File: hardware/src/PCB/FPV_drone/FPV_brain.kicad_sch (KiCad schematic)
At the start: 33 parts, among them IC2 STM32H743VIT6, IC3 USBLC6-2SC6, J1 TYPE-C-31-M-12, J3 Flash-pads, Y1 ABM3B-8.000MHZ-10-D1G-T

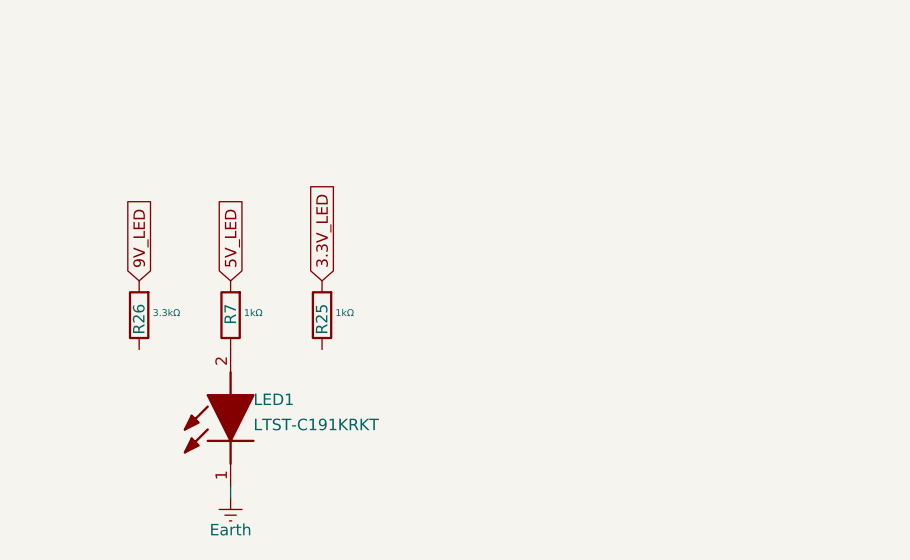
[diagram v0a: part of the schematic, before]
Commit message: added some leds
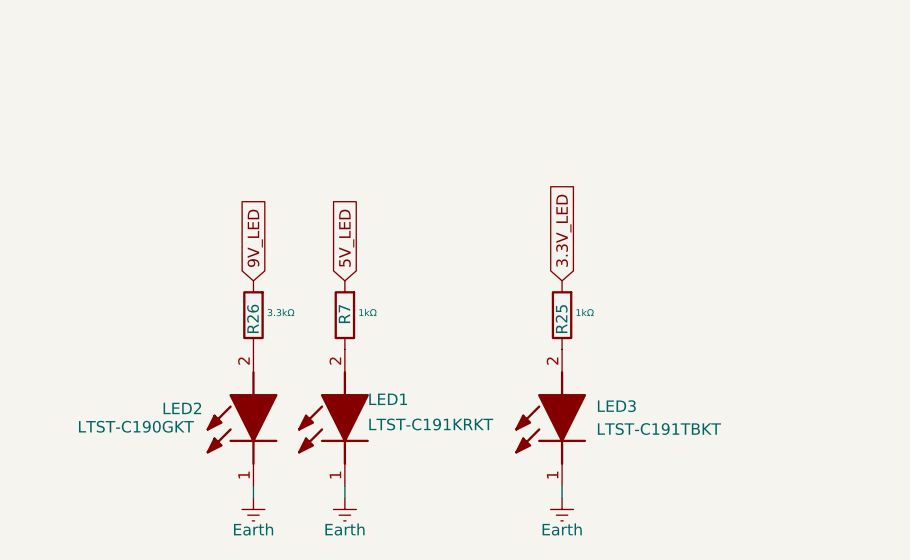
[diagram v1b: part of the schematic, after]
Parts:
- added LED2: LTST-C190GKT, LEDC1608X90N, symbol lib:LTST-C190GKT
- added LED3: LTST-C191TBKT, LEDC1608X65N, symbol lib:LTST-C191TBKT
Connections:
- net Earth: now also LED2.1 (K), LED3.1 (K)
- net at R26.1: now also LED2.2 (A)
- net at R25.1: now also LED3.2 (A)
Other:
- moved on the sheet: LED1, R25, R26, R7

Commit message: Update: schem drone
power functions almost finish... i wish
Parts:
- removed IC3: USBLC6-2SC6, SOT95P280X145-6N, symbol lib:USBLC6-2SC6
- removed J1: TYPE-C-31-M-12, TYPE-C-31-M-12:HRO_TYPE-C-31-M-12, symbol lib:TYPE-C-31-M-12
- removed J3: Flash-pads, symbol Connector_Generic:Conn_01x05
- removed R1, R2: 5.1kΩ, symbol Device:R
- added H1, H2, H3, H4: MountingHole_Pad, symbol Mechanical:MountingHole_Pad
- added TP1, TP2, TP3, TP4, TP5: TestPoint, symbol Connector:TestPoint
- C1, C2: value 15pF -> 12pF
- FB1: value BLM18BD421SZ1D (inductance) -> 220Ω @ 100MHz
- R12, R17: value 100Ω -> 10kΩ
- R25: value 1kΩ -> 680Ω
- R26: value 3.3kΩ -> 4.7kΩ
- R7: value 1kΩ -> 2.2kΩ
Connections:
- net 3.3V_LED is gone; now on net MCU_LED: R25.2
- net +3.3V: now also IC2.6 (VBAT), TP4.1
- net Earth: now also H1.1, H2.1, H3.1, H4.1, TP5.1
- net NRST: now also TP3.1
- net SWCLK: now also TP2.1
- net SWDIO: now also TP1.1
- net MCU_LED: now reaches IC2.34 (PB0)
- net 5V_LED renamed +5V
- net 9V_LED renamed +9V
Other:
- moved on the sheet: C1, C10, C11, C2, C22, C23, C24, C3, C4, C5, C6, C7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

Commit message: Update: schem almost finish
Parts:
- removed C22, C23, C24: 100nF, Capacitor_THT:C_Disc_D3.0mm_W2.0mm_P2.50mm, symbol PCM_SL_Devices:Capacitor_NP
- removed FB1: 220Ω @ 100MHz, BLM18SP221SN1B, symbol lib:BLM18BD421SZ1D
- removed R12, R17, R8: 10kΩ, symbol Device:R
- added C54: 100nF, Capacitor_THT:C_Disc_D3.0mm_W2.0mm_P2.50mm, symbol PCM_SL_Devices:Capacitor_NP
- added FB1: 220Ω @ 100MHz, BLM18SP221SN1B, symbol Device:L
- added J10, J7, J8, J9: JST_1mm_3, PCM_SparkFun-Connector:JST_1x03_P1.0mm_Horizontal_SMD, symbol PCM_SparkFun-Connector:Conn_01x03_JST_P1.0mm_Horizontal_SMD
- added J2: Conn_01x08, PCM_SparkFun-Connector:JST_1x08_P1.0mm_Horizontal_SMD, symbol PCM_SparkFun-Connector:Conn_01x08_JST_P1.0mm_Horizontal_SMD
- added J4: JST_1mm_4, PCM_SparkFun-Connector:JST_1x04_P1.0mm_Horizontal_SMD, symbol PCM_SparkFun-Connector:Conn_01x04_JST_P1.0mm_Horizontal_SMD
- added NT2: NetTie_4_Cross, symbol Device:NetTie_4_Cross
- added R40: 47Ω, symbol Device:R
- added R41: 10kΩ, symbol Device:R
- R25: value 680Ω -> 220Ω
- R26: value 4.7kΩ -> 1.1kΩ
- R7: value 2.2kΩ -> 620Ω
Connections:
- net +3.3V: now also FB1.1, R41.1
- net +5V: now also J4.3
- net Earth: now also C54.2, J2.1, J4.4, NT2.3; no longer IC2.19 (VSSA)
- net IBAT: now also IC2.25 (PA3)
- net ISC_IN: now also C1.2, Y1.1 (XTAL_1); no longer C2.1, Y1.3 (XTAL_2)
- net ISC_OUT: now also C2.1, Y1.3 (XTAL_2); no longer C1.2, Y1.1 (XTAL_1)
- net VBAT: now also IC2.24 (PA2)
- net at LED3.2 (A): now also R26.1; no longer R25.1
- net at LED2.2 (A): now also R25.1; no longer R26.1
- net CURR: now reaches IC2.15 (PC0)
- net CURR: now also J2.8
- net VDDA: now reaches IC2.21 (VDDA)
- net VDDA: now also FB1.2, R40.1; no longer IC2.20 (VREF+)
- net IMU1_CS: now reaches IC2.28 (PA4)
- net IMU1_SCLK: now reaches IC2.29 (PA5)
- net IMU1_SDO: now reaches IC2.30 (PA6)
- net IMU1_SDIO: now reaches IC2.31 (PA7)
- net IMU1_INT: now reaches IC2.32 (PC4)
- net IMU2_CS: now reaches IC2.35 (PB1)
- net IMU2_INT: now reaches IC2.36 (PB2)
- net IMU2_SCLK: now reaches IC2.42 (PE12)
- net IMU2_SDO: now reaches IC2.43 (PE13)
- net IMU2_SDIO: now reaches IC2.44 (PE14)
- net SCL: now reaches IC2.46 (PB10)
- net SDA: now reaches IC2.47 (PB11)
- net OSD_CS: now reaches IC2.51 (PB12)
- net OSD_SCK: now reaches IC2.52 (PB13)
- net OSD_MISO: now reaches IC2.53 (PB14)
- net OSD_MOSI: now reaches IC2.54 (PB15)
- net DJI_TX: now reaches IC2.55 (PD8)
- net DJI_RX: now reaches IC2.56 (PD9)
- net MOTOR_1: now reaches IC2.59 (PD12)
- net MOTOR_1: now also J2.3
- net MOTOR_2: now reaches IC2.60 (PD13)
- net MOTOR_2: now also J2.4
- net MOTOR_3: now reaches IC2.61 (PD14)
- net MOTOR_3: now also J2.5
- net MOTOR_4: now reaches IC2.62 (PD15)
- net MOTOR_4: now also J2.6
- net flash_CS: now reaches IC2.77 (PA15)
- net flash_CLK: now reaches IC2.78 (PC10)
- net flash_MISO: now reaches IC2.79 (PC11)
- net flash_MOSI: now reaches IC2.80 (PC12)
- net RADIO_RX: now reaches IC2.81 (PD0)
- net RADIO_RX: now also J4.2
- net RADIO_TX: now reaches IC2.82 (PD1)
- net RADIO_TX: now also J4.1
- net DJI_SBUS: now reaches IC2.87 (PD6)
- net TELE: now reaches IC2.93 (PB7)
- net TELE: now also J2.7
- net NRST renamed B_NRST
- net B_NRST: now also C54.1, R41.2
- new net BATT+: J2.2
- new net GNDA: IC2.19 (VSSA), NT2.2
- new net GNDD: NT2.4
- new net GNDPWR: NT2.1
- new net VREF: IC2.20 (VREF+), R40.2
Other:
- note added: "Advanced VDDA filtering"
- note added: "Blue - 9V Red - 5V Green - MCU (3.3V)"
- note added: "CL_reel = (C1*C2)/(C1+C2) + C_stray = (12*12)/(12+12) + ~3pF = 6 + 3 = 9-10 pF"
- note added: "Connectors"
- note added: "Crystal 0scillator - 8MHz +/-10ppm 200Ω 10pF"
- note added: "Info LEDS"
- note added: "Microcontroller - STM32H743VIT6"
- note added: "Mounting Holes"
- note added: "NRST button logic"
- moved on the sheet: C1, C10, C11, C2, C3, C4, C5, C6, C7, C8, C9, H1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

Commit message: Update: bit changes
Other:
- moved on the sheet: NT2
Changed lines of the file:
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@@
 	(wire
 		(pts
-			(xy 104.14 146.05) (xy 105.41 146.05)
+			(xy 77.47 143.51) (xy 78.74 143.51)
 		)
 		(stroke
@@
 	(wire
 		(pts
-			(xy 107.95 142.24) (xy 107.95 143.51)
+			(xy 81.28 139.7) (xy 81.28 140.97)
 		)
 		(stroke
@@
 	(wire
 		(pts
-			(xy 110.49 146.05) (xy 111.76 146.05)
+			(xy 83.82 143.51) (xy 85.09 143.51)
 		)
 		(stroke
@@
 	(wire
 		(pts
-			(xy 107.95 148.59) (xy 107.95 149.86)
+			(xy 81.28 146.05) (xy 81.28 147.32)
 		)
 		(stroke
@@
 	(symbol
 		(lib_id "power:Earth")
-		(at 107.95 142.24 180)
+		(at 81.28 139.7 180)
 		(unit 1)
 		(body_style 1)
@@
 		(dnp no)
 		(property "Reference" "#PWR0114"
-			(at 107.95 135.89 0)
+			(at 81.28 133.35 0)
 			(hide yes)
 			(show_name no)
@@
 		)
 		(property "Value" "Earth"
-			(at 107.95 138.684 0)
+			(at 81.28 136.144 0)
 			(show_name no)
 			(do_not_autoplace no)
@@
 		)
 		(property "Footprint" ""
-			(at 107.95 142.24 0)
+			(at 81.28 139.7 0)
 			(hide yes)
 			(show_name no)
@@
 		)
 		(property "Datasheet" ""
-			(at 107.95 142.24 0)
+			(at 81.28 139.7 0)
 			(hide yes)
 			(show_name no)
@@
 		)
 		(property "Description" "Power symbol creates a global label with name \"Earth\""
-			(at 107.95 142.24 0)
+			(at 81.28 139.7 0)
 			(hide yes)
 			(show_name no)
@@
 	(symbol
 		(lib_id "Device:NetTie_4_Cross")
-		(at 107.95 146.05 0)
+		(at 81.28 143.51 0)
 		(unit 1)
 		(body_style 1)
@@
 		(dnp no)
 		(property "Reference" "NT2"
-			(at 103.124 150.114 0)
+			(at 76.454 147.574 0)
 			(show_name no)
 			(do_not_autoplace no)
@@
 		)
 		(property "Value" "NetTie_4_Cross"
-			(at 118.11 143.6368 0)
+			(at 91.44 141.0968 0)
 			(hide yes)
 			(show_name no)
@@
 		)
 		(property "Footprint" ""
-			(at 107.95 146.05 0)
+			(at 81.28 143.51 0)
 			(hide yes)
 			(show_name no)
@@
 		)
 		(property "Datasheet" ""
-			(at 107.95 146.05 0)
+			(at 81.28 143.51 0)
 			(hide yes)
 			(show_name no)
@@
 		)
 		(property "Description" "Net tie, 4 pins, cross"
-			(at 107.95 146.05 0)
+			(at 81.28 143.51 0)
 			(hide yes)
 			(show_name no)
@@
 	(symbol
 		(lib_id "power:GNDD")
-		(at 107.95 149.86 0)
+		(at 81.28 147.32 0)
 		(unit 1)
 		(body_style 1)
@@
 		(dnp no)
 		(property "Reference" "#PWR0117"
-			(at 107.95 156.21 0)
+			(at 81.28 153.67 0)
 			(hide yes)
 			(show_name no)
@@
 		)
 		(property "Value" "GNDD"
-			(at 107.95 153.162 0)
+			(at 81.28 150.622 0)
 			(show_name no)
 			(do_not_autoplace no)
@@
 		)
 		(property "Footprint" ""
-			(at 107.95 149.86 0)
+			(at 81.28 147.32 0)
 			(hide yes)
 			(show_name no)
@@
 		)
 		(property "Datasheet" ""
-			(at 107.95 149.86 0)
+			(at 81.28 147.32 0)
 			(hide yes)
 			(show_name no)
@@
 		)
 		(property "Description" "Power symbol creates a global label with name \"GNDD\" , digital ground"
-			(at 107.95 149.86 0)
+			(at 81.28 147.32 0)
 			(hide yes)
 			(show_name no)
@@
 	(symbol
 		(lib_id "power:GNDPWR")
-		(at 104.14 146.05 270)
+		(at 77.47 143.51 270)
 		(unit 1)
 		(body_style 1)
@@
 		(dnp no)
 		(property "Reference" "#PWR0118"
-			(at 99.06 146.05 0)
+			(at 72.39 143.51 0)
 			(hide yes)
 			(show_name no)
@@
 		)
 		(property "Value" "GNDPWR"
-			(at 98.298 145.796 90)
+			(at 71.628 143.256 90)
 			(show_name no)
 			(do_not_autoplace no)
@@
 		)
 		(property "Footprint" ""
-			(at 102.87 146.05 0)
+			(at 76.2 143.51 0)
 			(hide yes)
 			(show_name no)
@@
 		)
 		(property "Datasheet" ""
-			(at 102.87 146.05 0)
+			(at 76.2 143.51 0)
 			(hide yes)
 			(show_name no)
@@
 		)
 		(property "Description" "Power symbol creates a global label with name \"GNDPWR\" , global ground"
-			(at 104.14 146.05 0)
+			(at 77.47 143.51 0)
 			(hide yes)
 			(show_name no)
@@
 	(symbol
 		(lib_id "power:GNDA")
-		(at 111.76 146.05 90)
+		(at 85.09 143.51 90)
 		(unit 1)
 		(body_style 1)
@@
 		(dnp no)
 		(property "Reference" "#PWR0119"
-			(at 118.11 146.05 0)
+			(at 91.44 143.51 0)
 			(hide yes)
 			(show_name no)
@@
 		)
 		(property "Value" "GNDA"
-			(at 116.586 146.05 90)
+			(at 89.916 143.51 90)
 			(show_name no)
 			(do_not_autoplace no)
@@
 		)
 		(property "Footprint" ""
-			(at 111.76 146.05 0)
+			(at 85.09 143.51 0)
 			(hide yes)
 			(show_name no)
@@
 		)
 		(property "Datasheet" ""
-			(at 111.76 146.05 0)
+			(at 85.09 143.51 0)
 			(hide yes)
 			(show_name no)
@@
 		)
 		(property "Description" "Power symbol creates a global label with name \"GNDA\" , analog ground"
-			(at 111.76 146.05 0)
+			(at 85.09 143.51 0)
 			(hide yes)
 			(show_name no)

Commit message: update: schem finished
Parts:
- removed C11: 1uF, Capacitor_THT:C_Disc_D3.0mm_W2.0mm_P2.50mm, symbol PCM_SL_Devices:Capacitor_NP
- removed FB1: 220Ω @ 100MHz, BLM18SP221SN1B, symbol Device:L
- removed IC2: STM32H743VIT6, QFP50P1600X1600X160-100N, symbol lib:STM32H743VIT6
- removed R9: 10kΩ, symbol Device:R
- added C14: 2.2uF, Capacitor_THT:C_Disc_D3.0mm_W2.0mm_P2.50mm, symbol PCM_SL_Devices:Capacitor_NP
- added L3: STM32H743VIH6, LIB:BGA100C80P10X10_800X800X110, symbol lib:STM32H743VIH6
- C10: value 100nF -> 1uF
- C5: value 2.2uF -> 4.7uF
- H1, H2, H3, H4: footprint (none) -> MountingHole:MountingHole_3.2mm_M3_ISO7380_Pad_TopBottom
- LED1: footprint LEDC1608X55N -> LIB:LEDC1608X55N
- LED2: footprint LEDC1608X90N -> LIB:LEDC1608X90N
- LED3: footprint LEDC1608X65N -> LIB:LEDC1608X65N
- NT2: footprint (none) -> NetTie:NetTie-4_SMD_Pad0.5mm
- R40: value 47Ω -> 10kΩ
- S2: footprint EVQ-P7A01P:SW_EVQ-P7A01P -> LIB:SW_EVQ-P7A01P
- TP1, TP2, TP3, TP4, TP5: footprint (none) -> TestPoint:TestPoint_Pad_D1.0mm
- Y1: footprint ABM3B -> LIB:ABM3B
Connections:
- net VDDA is gone; now on net Earth: R40.1
- net VREF is gone; now on net STM_BOOT0: R40.2
- net +3.3V: now also C10.1, C4.1, C5.1, C8.1, C9.1, L3.B2 (VBAT), L3.D2 (VDD_1), L3.F4 (VDDLDO), L3.F5 (VDD_2), L3.F6 (VDD33USB), L3.F7 (PDR_ON), L3.H1 (VDDA), L3.K1 (VDD_3); no longer C10.2, C4.2, C8.2, C9.2
- net +5V: now also J10.1, J7.1, J8.1, J9.1
- net B_NRST: now also L3.E1 (NRST)
- net CURR: now also L3.F1 (PC0)
- net DJI_RX: now also L3.J9 (PD9)
- net DJI_SBUS: now also L3.C6 (PD6)
- net DJI_TX: now also L3.K9 (PD8)
- net Earth: now also C10.2, C4.2, C5.2, C8.2, C9.2, J10.2, J7.2, J8.2, J9.2, C14.1, L3.C2 (VSS_1), L3.E4 (VSS_2), L3.E5 (VSS_3), L3.E6 (VSS_4), L3.G1 (VSSA), L3.J1 (VSS_5); no longer C10.1, C4.1, C5.1, C8.1, C9.1
- net IBAT: now also L3.K2 (PA3)
- net IMU1_CS: now also L3.G3 (PA4)
- net IMU1_INT: now also L3.G4 (PC4)
- net IMU1_SCLK: now also L3.H3 (PA5)
- net IMU1_SDIO: now also L3.K3 (PA7)
- net IMU1_SDO: now also L3.J3 (PA6)
- net IMU2_CS: now also L3.K4 (PB1)
- net IMU2_INT: now also L3.G5 (PB2)
- net IMU2_SCLK: now also L3.J6 (PE12)
- net IMU2_SDIO: now also L3.G7 (PE14)
- net IMU2_SDO: now also L3.K6 (PE13)
- net ISC_IN: now also L3.C1 (PH0-OSC_IN)
- net ISC_OUT: now also L3.D1 (PH1-OSC_OUT)
- net MCU_LED: now also L3.J4 (PB0)
- net MOTOR_1: now also L3.K10 (PD12)
- net MOTOR_2: now also L3.J10 (PD13)
- net MOTOR_3: now also L3.H8 (PD14)
- net MOTOR_4: now also L3.G8 (PD15)
- net OSD_CS: now also L3.K8 (PB12)
- net OSD_MISO: now also L3.H10 (PB14)
- net OSD_MOSI: now also L3.G10 (PB15)
- net OSD_SCK: now also L3.J8 (PB13)
- net RADIO_RX: now also L3.D8 (PD0)
- net RADIO_TX: now also L3.E8 (PD1)
- net SCL: now also L3.J7 (PB10)
- net SDA: now also L3.K7 (PB11)
- net STM_BOOT0: now also L3.D5 (BOOT0)
- net SWCLK: now also L3.A9 (PA14)
- net SWDIO: now also L3.A10 (PA13)
- net TELE: now also L3.A5 (PB7)
- net VBAT: now also L3.J2 (PA2)
- net flash_CLK: now also L3.B9 (PC10)
- net flash_CS: now also L3.A8 (PA15)
- net flash_MISO: now also L3.B8 (PC11)
- net flash_MOSI: now also L3.C8 (PC12)
- net LED_DATA2: now reaches J8.3
- net LED_DATA2: now also L3.B7 (PD2)
- net VCAP1: now reaches C6.2
- net VCAP1: now also L3.E7 (VCAP_1)
- net LED_DATA4: now reaches J10.3
- net LED_DATA4: now also L3.H7 (PE15)
- net at R4.1: now also L3.C10 (PA11)
- net at R3.1: now also L3.B10 (PA12)
- net LED_DATA3: now reaches J9.3
- net LED_DATA3: now also L3.H2 (PA1)
- net LED_DATA1: now reaches J7.3
- net LED_DATA1: now also L3.C4 (PE1)
- new net CAM_C: L3.B4 (PB8)
- new net IRC: L3.C9 (PA9)
- new net VCAP2: C14.2, L3.F8 (VCAP_2)
- no-connect marks 2 -> 36
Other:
- note added: "Microcontroller - Decoupling VCAP"
- note added: "Microcontroller - STM32H743VIH6"
- note removed: "Microcontroller - STM32H743VIT6"
- moved on the sheet: C6, J10, J7, J8, J9, S2

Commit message: Update: schem finished
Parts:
- removed J10, J9: JST_1mm_3, PCM_SparkFun-Connector:JST_1x03_P1.0mm_Horizontal_SMD, symbol PCM_SparkFun-Connector:Conn_01x03_JST_P1.0mm_Horizontal_SMD
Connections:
- net B_NRST renamed NRST
- net LED_DATA3: no longer names the net of L3.H2 (PA1)
- net LED_DATA4: no longer names the net of L3.H7 (PE15)
- no-connect marks 36 -> 38
